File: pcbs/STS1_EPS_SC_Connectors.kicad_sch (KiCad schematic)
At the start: 17 parts, among them J2 Panel Y-, J4 Panel Y+, J5 Panel Z-, J6 Panel Z+, J7 Panel X+, U25 TPS259472ARPW, U26 TPS259472ARPW, U29 TPS259472ARPW

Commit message: STS1_EPS_1 now without errors.
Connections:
- net Panel_Y-_5: no longer D15.5
- net Panel_Y-_6: now also D15.5; no longer D15.6
- net Panel_Y-_7: now also D15.6; no longer D15.7
- net Panel_Y-_8: now also D15.7
- net Panel_Z-_5: no longer D16.5
- net Panel_Z-_6: now also D16.5; no longer D16.6
- net Panel_Z-_7: now also D16.6; no longer D16.7
- net Panel_Z-_8: now also D16.7
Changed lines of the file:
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@@
 		)
 	)
-	(label "Panel_Y-_6"
+	(label "Panel_Y-_7"
 		(at 139.7 92.71 0)
 		(fields_autoplaced yes)
@@
 		)
 	)
-	(label "Panel_Z-_7"
+	(label "Panel_Z-_8"
 		(at 129.54 144.78 180)
 		(fields_autoplaced yes)
@@
 		)
 	)
-	(label "Panel_Y-_7"
+	(label "Panel_Y-_8"
 		(at 129.54 95.25 180)
 		(fields_autoplaced yes)
@@
 		)
 	)
-	(label "Panel_Y-_5"
+	(label "Panel_Y-_6"
 		(at 129.54 92.71 180)
 		(fields_autoplaced yes)
@@
 		)
 	)
-	(label "Panel_Z-_5"
+	(label "Panel_Z-_6"
 		(at 129.54 142.24 180)
 		(fields_autoplaced yes)
@@
 		)
 	)
-	(label "Panel_Z-_6"
+	(label "Panel_Z-_7"
 		(at 139.7 142.24 0)
 		(fields_autoplaced yes)

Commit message: Added part numbers for some ESD diodes.
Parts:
- D12, D14, D15, D16, D17: value ~ -> LLP1713-9L
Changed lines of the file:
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@@
 			)
 		)
-		(property "Value" "~"
+		(property "Value" "LLP1713-9L"
 			(at 134.62 110.49 0)
 			(effects
@@
 			)
 		)
-		(property "Value" "~"
+		(property "Value" "LLP1713-9L"
 			(at 134.62 85.09 0)
 			(effects
@@
 			)
 		)
-		(property "Value" "~"
+		(property "Value" "LLP1713-9L"
 			(at 134.62 60.96 0)
 			(effects
@@
 			)
 		)
-		(property "Value" "~"
+		(property "Value" "LLP1713-9L"
 			(at 134.62 134.62 0)
 			(effects
@@
 			)
 		)
-		(property "Value" "~"
+		(property "Value" "LLP1713-9L"
 			(at 134.62 161.29 0)
 			(effects

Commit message: Fixed diode values for good.
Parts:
- D12, D14, D15, D16, D17: value LLP1713-9L -> VESD05A8A-HNH-GS08
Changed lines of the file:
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@@
 			)
 		)
-		(property "Value" "LLP1713-9L"
+		(property "Value" "VESD05A8A-HNH-GS08"
 			(at 134.62 110.49 0)
 			(effects
@@
 			)
 		)
-		(property "Value" "LLP1713-9L"
+		(property "Value" "VESD05A8A-HNH-GS08"
 			(at 134.62 85.09 0)
 			(effects
@@
 			)
 		)
-		(property "Value" "LLP1713-9L"
+		(property "Value" "VESD05A8A-HNH-GS08"
 			(at 134.62 60.96 0)
 			(effects
@@
 			)
 		)
-		(property "Value" "LLP1713-9L"
+		(property "Value" "VESD05A8A-HNH-GS08"
 			(at 134.62 134.62 0)
 			(effects
@@
 			)
 		)
-		(property "Value" "LLP1713-9L"
+		(property "Value" "VESD05A8A-HNH-GS08"
 			(at 134.62 161.29 0)
 			(effects

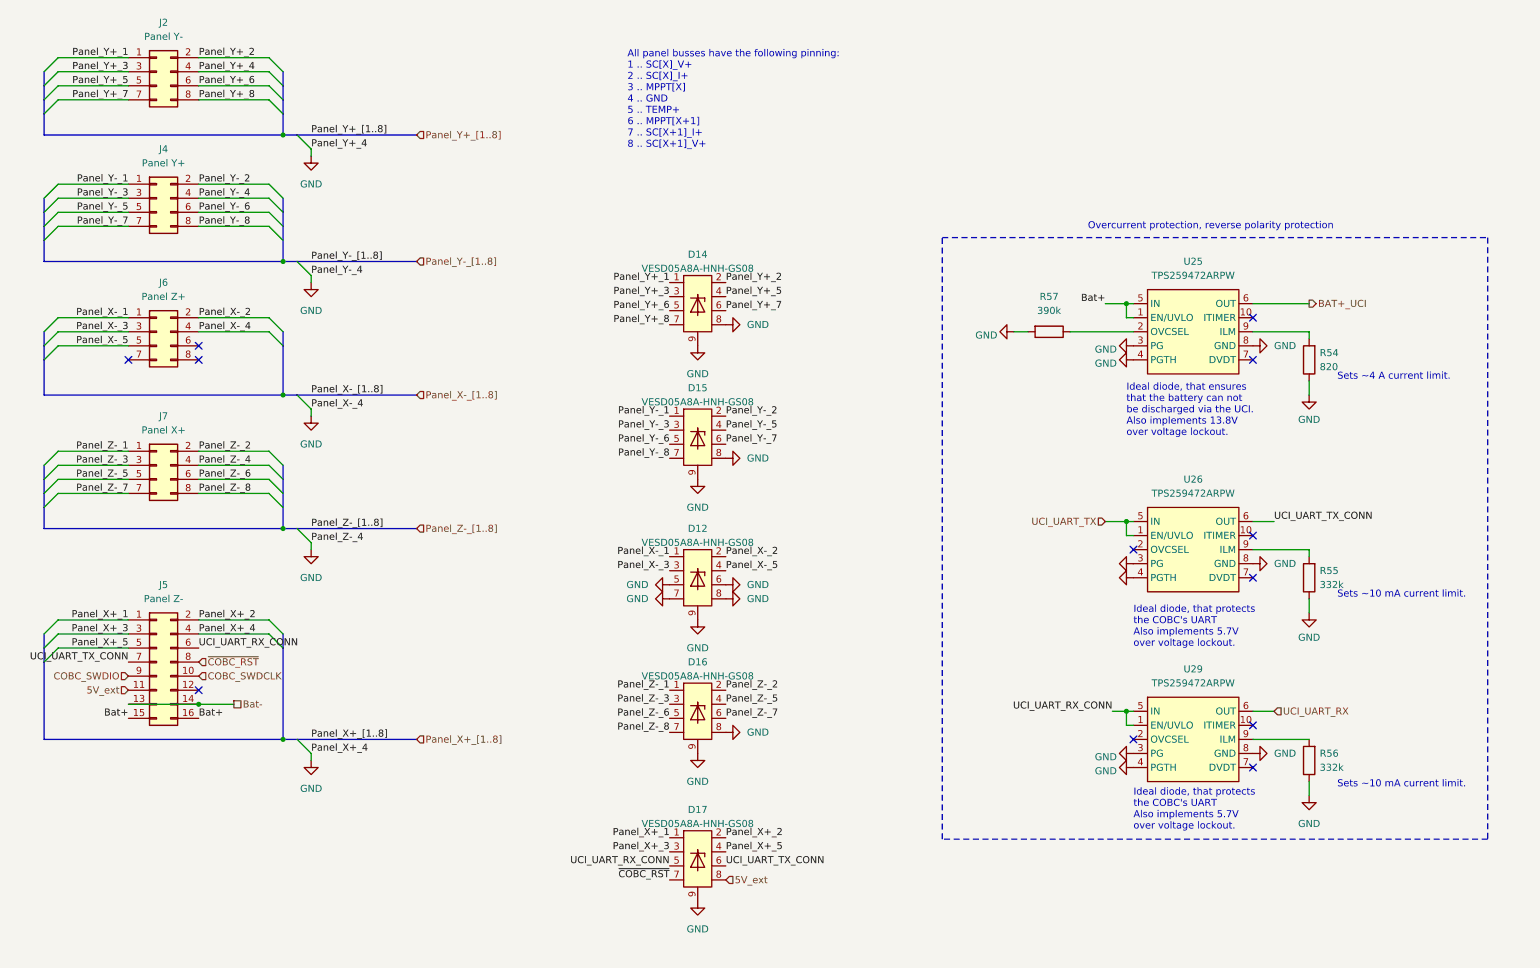
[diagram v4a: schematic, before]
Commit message: Made the label names at the UCI connector more consistent.
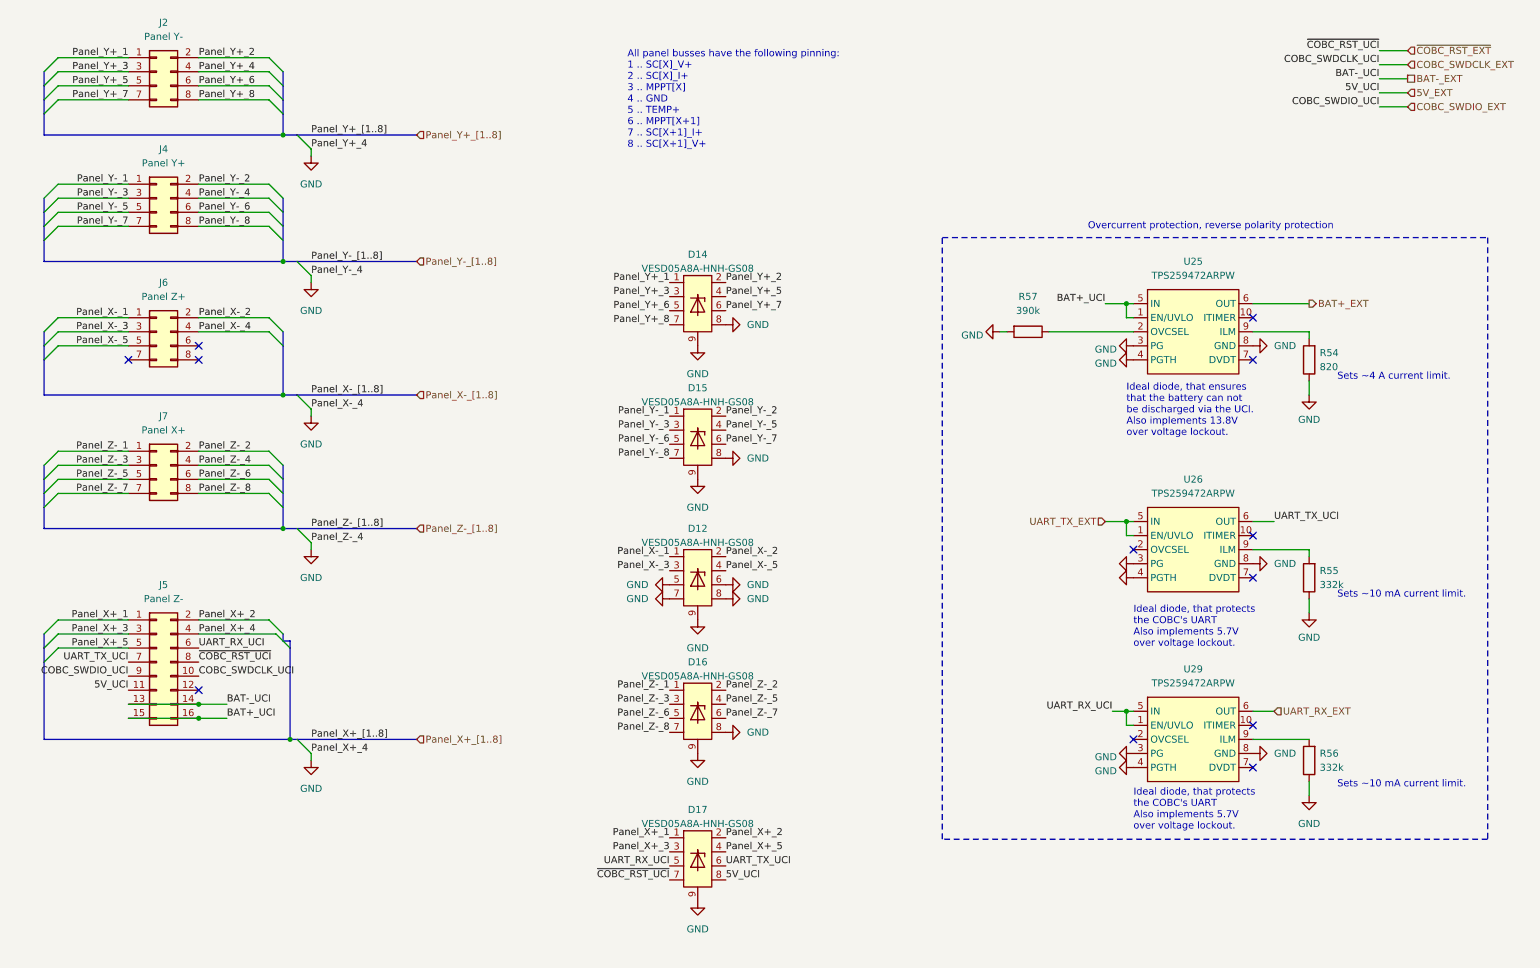
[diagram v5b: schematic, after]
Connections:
- net Bat+ is gone; now on net BAT+_UCI: J5.15 (Pin_15), J5.16 (Pin_16), U25.1 (EN/UVLO), U25.5 (IN)
- net BAT+_UCI: no longer U25.6 (OUT)
- net 5V_ext renamed 5V_EXT
- net Bat- renamed BAT-_EXT
- net COBC_SWDCLK renamed COBC_SWDCLK_EXT
- net COBC_SWDIO renamed COBC_SWDIO_EXT
- net UCI_UART_RX renamed UART_RX_EXT
- net UCI_UART_RX_CONN renamed UART_RX_UCI
- net UCI_UART_TX renamed UART_TX_EXT
- net UCI_UART_TX_CONN renamed UART_TX_UCI
- net ~{COBC_RST} renamed ~{COBC_RST_EXT}
- new net BAT+_EXT: U25.6 (OUT)
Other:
- moved on the sheet: R57

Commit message: Removed the ideal diodes at the UCI UART RX/TX lines. Added TVS diodes to those lines.
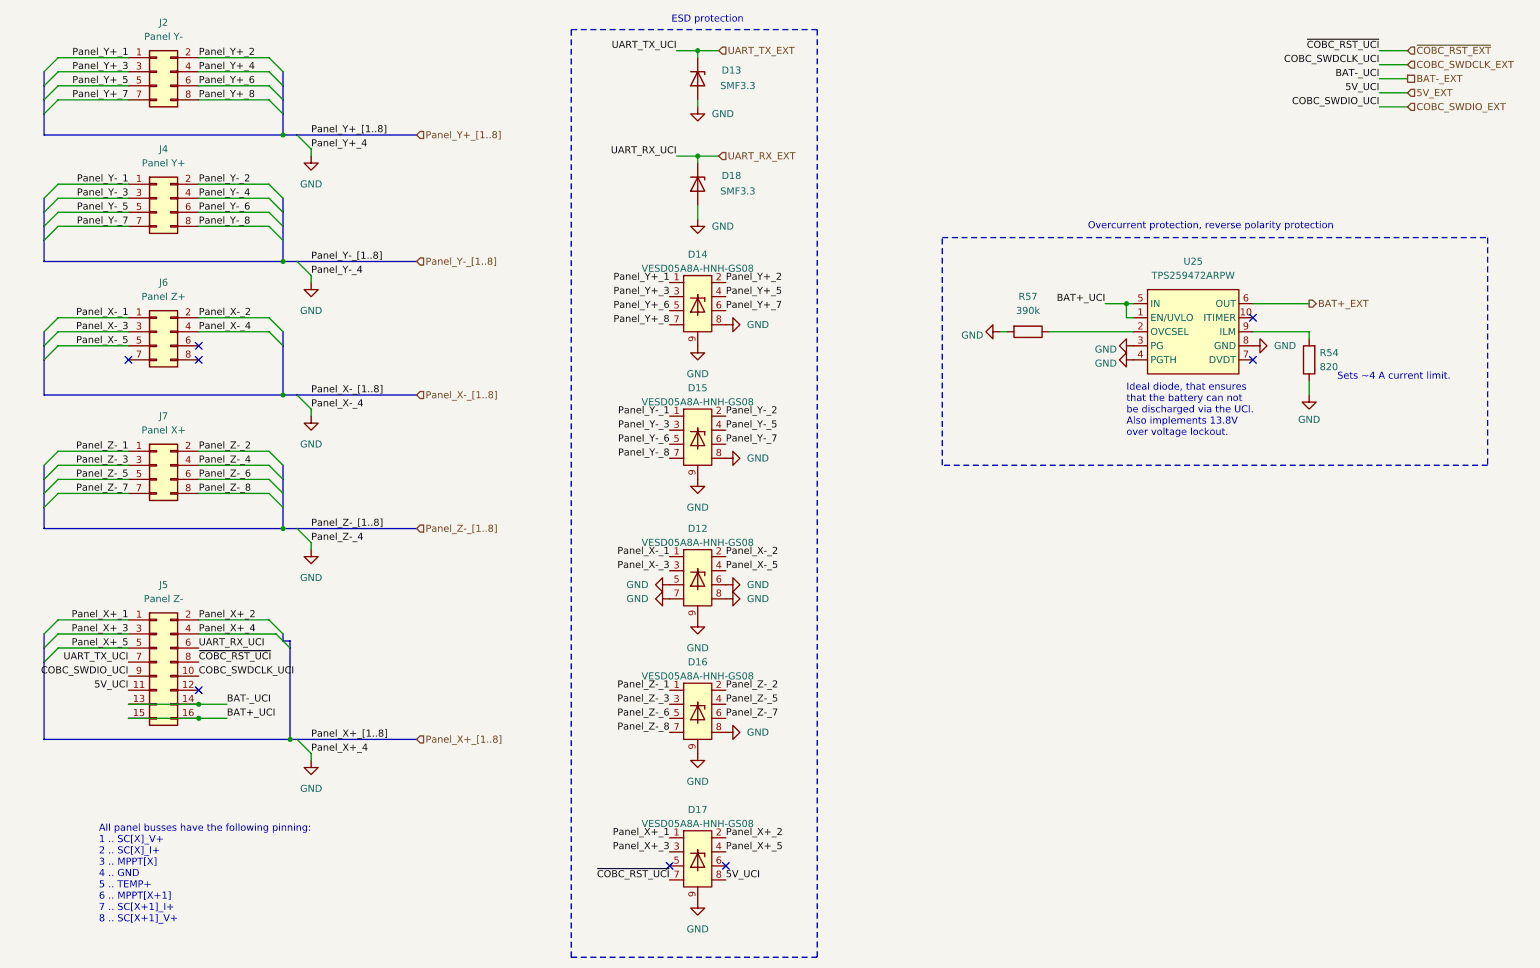
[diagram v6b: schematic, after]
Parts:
- removed R55, R56: 332k, Resistor_SMD:R_0805_2012Metric, symbol Device:R
- removed U26, U29: TPS259472ARPW, STS_Package_DFN_QFN:TPS259472ARPWR, symbol STS_Power_Management:TPS259472ARPW
- added D13, D18: SMF3.3, Diode_SMD:D_SOD-123, symbol Device:D_Zener
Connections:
- net GND: now also D13.2 (A), D18.2 (A)
- net UART_RX_EXT: now also J5.6 (Pin_6), D18.1 (K)
- net UART_TX_EXT: now also J5.7 (Pin_7), D13.1 (K)
- net UART_RX_UCI: no longer names the net of D17.5
- net UART_RX_UCI: no longer J5.6 (Pin_6)
- net UART_TX_UCI: no longer names the net of D17.6
- net UART_TX_UCI: no longer J5.7 (Pin_7)
- no-connect marks 12 -> 8
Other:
- note added: "ESD protection"
- note removed: "Ideal diode, that protects the COBC's UART Also implements 5.7V over voltage lockout."
- note removed: "Sets ~10 mA current limit."

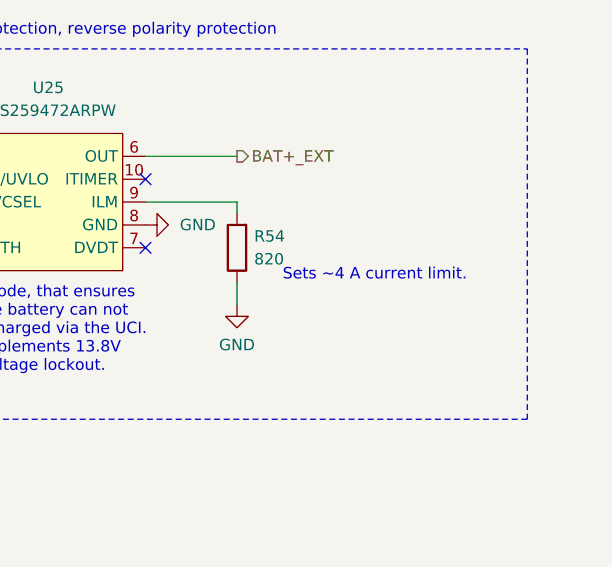
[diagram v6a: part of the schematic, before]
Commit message: Added tolerances to some resistors that should be precise.
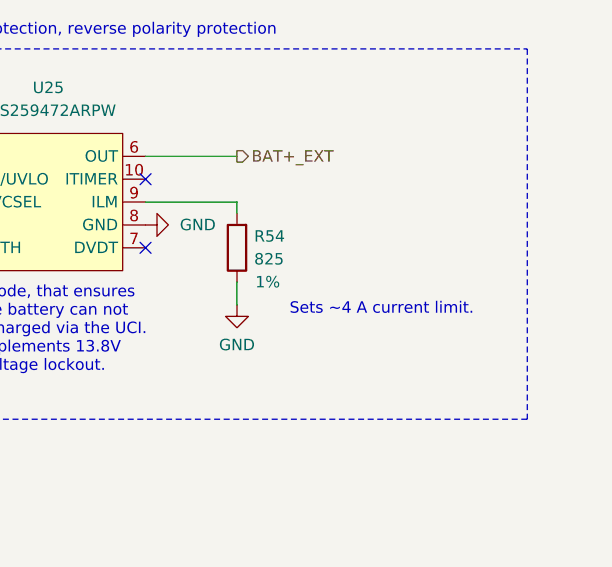
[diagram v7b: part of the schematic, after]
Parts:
- R54: value 820 -> 825; Tolerance (none) -> 1%
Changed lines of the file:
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@@
 	(text "Sets ~4 A current limit."
 		(exclude_from_sim no)
-		(at 250.19 81.28 0)
+		(at 250.952 85.09 0)
 		(effects
 			(font
@@
 		(on_board yes)
 		(dnp no)
-		(fields_autoplaced yes)
 		(property "Reference" "R54"
 			(at 247.015 76.1999 0)
@@
 			)
 		)
-		(property "Value" "820"
+		(property "Value" "825"
 			(at 247.015 78.7399 0)
 			(effects
@@
 			)
 		)
+		(property "Tolerance" "1%"
+			(at 247.142 81.28 0)
+			(effects
+				(font
+					(size 1.27 1.27)
+				)
+				(justify right)
+			)
+		)
